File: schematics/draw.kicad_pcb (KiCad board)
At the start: 2 copper layers, 50 x 40 mm, 38 parts, among them P1 I2C, P2 UART, P3 DBG, P4 USB_OTG, P5 Power_IN, P6 Power_OUT, SW1 SW_Push, U1 EFM32HG309, U2 TPD4E002, U3 INA260

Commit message: updated silkscreen bumped version
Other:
- board text added: "In"
- board text added: "Out"
- board text added: "draw v1.1 14/3/2017"
- board text added: "↑"
- board text removed: "draw v1.0 7/2/2017"
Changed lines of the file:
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@@
     (area 50.811981 93.5356 116.824543 136.5614)
     (thickness 1.6)
-    (drawings 22)
+    (drawings 25)
     (tracks 268)
     (zones 0)
@@
   (layers
     (0 F.Cu signal)
-    (31 B.Cu signal hide)
+    (31 B.Cu signal)
     (32 B.Adhes user)
     (33 F.Adhes user)
@@
       (xy 0.376964 2.709982)) (layer B.SilkS) (width 0.01))
   )
-  (gr_text "draw v1.0\n7/2/2017" (at 64.5922 124.4981) (layer B.SilkS)
+  (gr_text Out (at 63.119 105.791) (layer F.SilkS)
+    (effects (font (size 1.2 1.2) (thickness 0.3)))
+  )
+  (gr_text In (at 63.2079 125.5268) (layer F.SilkS)
+    (effects (font (size 1.2 1.2) (thickness 0.3)))
+  )
+  (gr_text ↑ (at 64.262 113.3221) (layer F.SilkS)
+    (effects (font (size 7.2 1.2) (thickness 0.3)))
+  )
+  (gr_text "draw v1.1\n14/3/2017" (at 64.5922 124.4981) (layer B.SilkS)
     (effects (font (size 0.8 0.8) (thickness 0.2)) (justify mirror))
   )

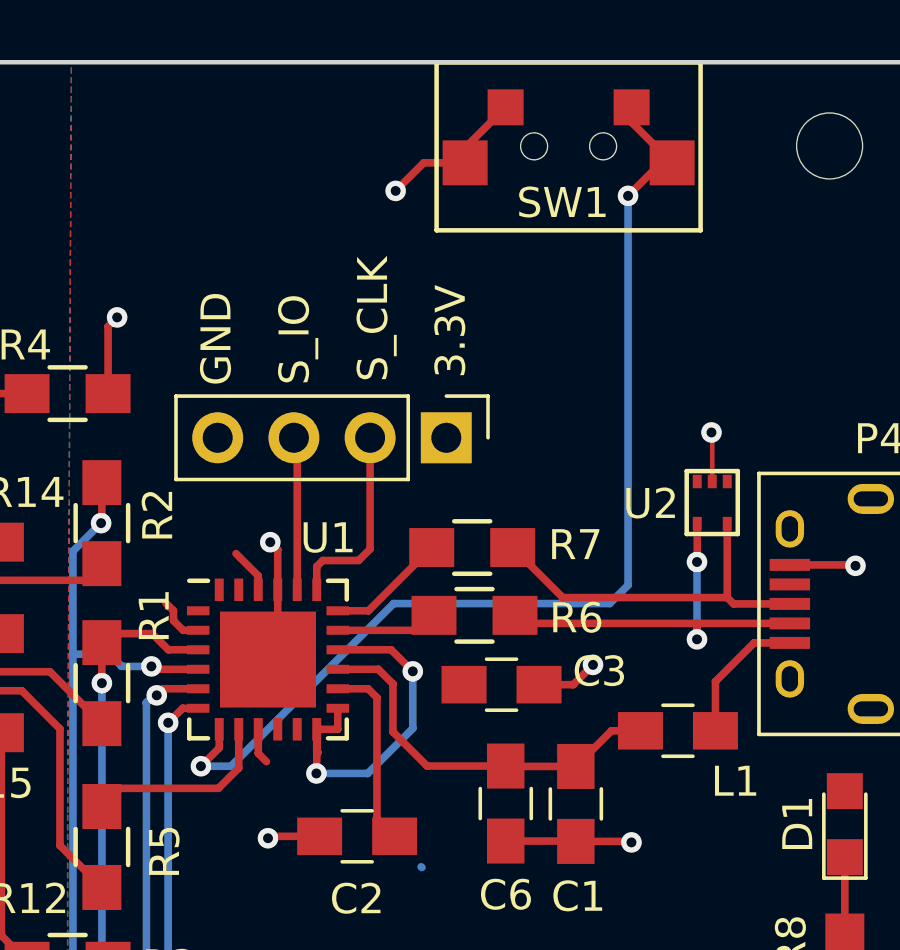
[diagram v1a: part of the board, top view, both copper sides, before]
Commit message: fixed the footprint for button
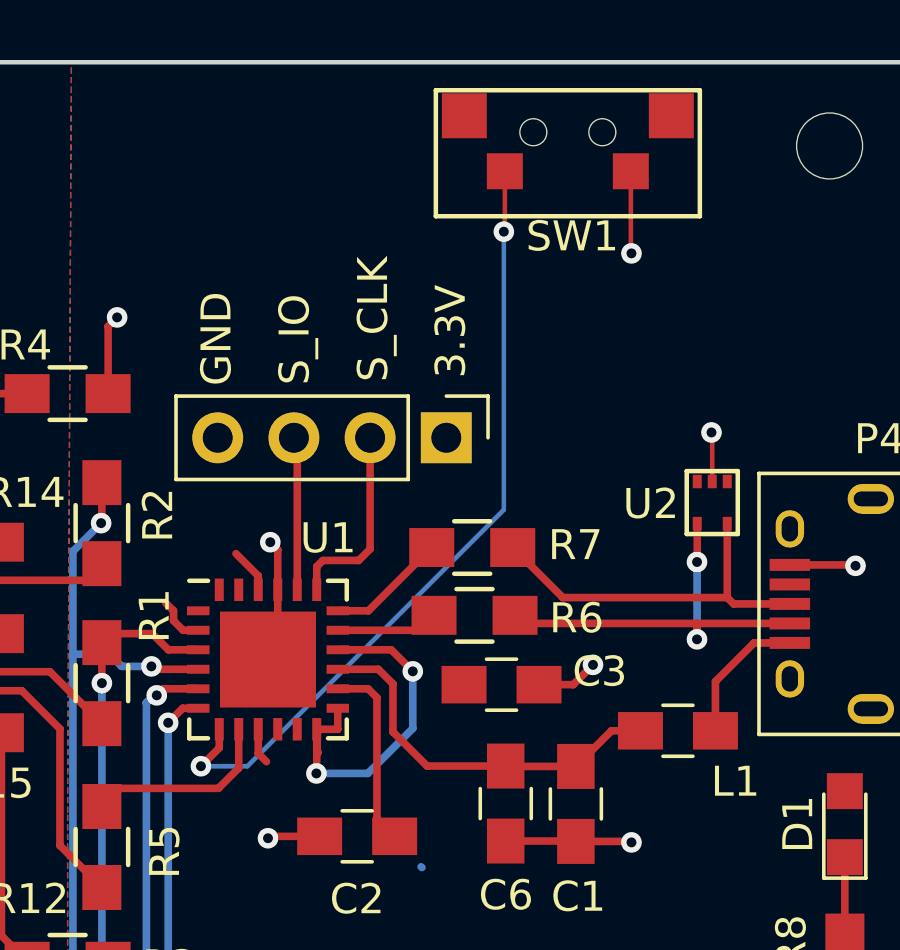
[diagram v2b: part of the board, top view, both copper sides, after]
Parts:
- SW1: footprint draw:HTB1 -> draw:Tact
- moved SW1 0.47 mm to (98.5, 97.3), turned to 0 degrees
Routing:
- net Net-(SW1-Pad1): track 35.6 -> 26.5 mm
- net GND: track 30.5 -> 28.1 mm
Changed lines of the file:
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@@
 (kicad_pcb (version 4) (host pcbnew 4.0.5)
   (general
-    (links 88)
+    (links 86)
     (no_connects 0)
     (area 50.811981 93.5356 116.824543 136.5614)
     (thickness 1.6)
     (drawings 25)
-    (tracks 268)
+    (tracks 261)
     (zones 0)
     (modules 38)
@@
   (page A4)
   (layers
-    (0 F.Cu signal)
+    (0 F.Cu signal hide)
     (31 B.Cu signal)
     (32 B.Adhes user)
@@
   )
   (setup
-    (last_trace_width 0.254)
+    (last_trace_width 0.1524)
     (user_trace_width 0.1524)
     (user_trace_width 1.1)
@@
     (add_net "Net-(U2-Pad3)")
     (add_net "Net-(U3-Pad13)")
-  )
-  (module draw:HTB1 (layer F.Cu)
-    (at 98.4885 97.8027 180)
-    (fp_text reference SW1 (at 0.1905 -1.8923 180) (layer F.SilkS)
-      (effects (font (size 1 1) (thickness 0.15)))
-    )
-    (fp_text value SW_Push (at 0 -1.905 180) (layer F.Fab) hide
-      (effects (font (size 1 1) (thickness 0.15)))
-    )
-    (fp_line (start -4.4 -2.8) (end 4.4 -2.8) (layer F.SilkS) (width 0.15))
-    (fp_line (start 4.4 -2.8) (end 4.4 2.8) (layer F.SilkS) (width 0.15))
-    (fp_line (start 4.4 2.8) (end -4.4 2.8) (layer F.SilkS) (width 0.15))
-    (fp_line (start -4.4 2.8) (end -4.4 -2.8) (layer F.SilkS) (width 0.15))
-    (pad 2 smd rect (at 3.45 -0.55 180) (size 1.5 1.5) (layers F.Cu F.Paste F.Mask)
-      (net 2 GND))
-    (pad "" np_thru_hole circle (at -1.15 0 180) (size 0.9 0.9) (drill 0.9) (layers *.Cu *.Mask))
-    (pad 2 smd rect (at 2.1 1.3 180) (size 1.2 1.2) (layers F.Cu F.Paste F.Mask)
-      (net 2 GND))
-    (pad 1 smd rect (at -2.1 1.3 180) (size 1.2 1.2) (layers F.Cu F.Paste F.Mask)
-      (net 25 "Net-(SW1-Pad1)"))
-    (pad "" np_thru_hole circle (at 1.15 0 180) (size 0.9 0.9) (drill 0.9) (layers *.Cu *.Mask))
-    (pad 1 smd rect (at -3.45 -0.55 180) (size 1.5 1.5) (layers F.Cu F.Paste F.Mask)
-      (net 25 "Net-(SW1-Pad1)"))
   )
   (module Resistors_SMD:R_0805_HandSoldering (layer F.Cu)
@@
       (xy 0.376964 2.709982)) (layer B.SilkS) (width 0.01))
   )
+  (module draw:Tact (layer F.Cu)
+    (at 98.4631 97.3328)
+    (fp_text reference SW1 (at 0.15 3.475) (layer F.SilkS)
+      (effects (font (size 1 1) (thickness 0.15)))
+    )
+    (fp_text value SW_Push (at -0.05 2) (layer F.Fab)
+      (effects (font (size 1 1) (thickness 0.15)))
+    )
+    (fp_line (start -4.4 -1.4) (end 4.4 -1.4) (layer F.SilkS) (width 0.15))
+    (fp_line (start 4.4 -1.4) (end 4.4 2.8) (layer F.SilkS) (width 0.15))
+    (fp_line (start 4.4 2.8) (end -4.4 2.8) (layer F.SilkS) (width 0.15))
+    (fp_line (start -4.4 2.8) (end -4.4 -1.4) (layer F.SilkS) (width 0.15))
+    (pad "" smd rect (at 3.45 -0.55) (size 1.5 1.5) (layers F.Cu F.Paste F.Mask))
+    (pad "" np_thru_hole circle (at -1.15 0) (size 0.9 0.9) (drill 0.9) (layers *.Cu *.Mask))
+    (pad 2 smd rect (at 2.1 1.3) (size 1.2 1.2) (layers F.Cu F.Paste F.Mask)
+      (net 2 GND))
+    (pad 1 smd rect (at -2.1 1.3) (size 1.2 1.2) (layers F.Cu F.Paste F.Mask)
+      (net 25 "Net-(SW1-Pad1)"))
+    (pad "" np_thru_hole circle (at 1.15 0) (size 0.9 0.9) (drill 0.9) (layers *.Cu *.Mask))
+    (pad "" smd rect (at -3.45 -0.55) (size 1.5 1.5) (layers F.Cu F.Paste F.Mask))
+  )
   (gr_text Out (at 63.119 105.791) (layer F.SilkS)
     (effects (font (size 1.2 1.2) (thickness 0.3)))
@@
   (segment (start 100.8834 117.2845) (end 99.9182 117.2845) (width 0.254) (layer F.Cu) (net 1))
   (segment (start 99.9182 117.2845) (end 98.7298 118.4729) (width 0.254) (layer F.Cu) (net 1))
-  (segment (start 95.0385 98.3527) (end 95.0385 97.8527) (width 0.254) (layer F.Cu) (net 2))
-  (segment (start 95.0385 97.8527) (end 96.3885 96.5027) (width 0.254) (layer F.Cu) (net 2))
-  (segment (start 95.0385 98.3527) (end 93.6586 98.3527) (width 0.254) (layer F.Cu) (net 2))
-  (segment (start 92.7227 99.2886) (end 92.7227 99.3394) (width 0.254) (layer B.Cu) (net 2))
-  (via (at 92.7227 99.2886) (size 0.6858) (drill 0.3302) (layers F.Cu B.Cu) (net 2))
-  (segment (start 93.6586 98.3527) (end 92.7227 99.2886) (width 0.254) (layer F.Cu) (net 2))
+  (segment (start 100.5631 98.6328) (end 100.5631 101.3505) (width 0.1524) (layer F.Cu) (net 2) (status 400000))
+  (via (at 100.584 101.3714) (size 0.6858) (drill 0.3302) (layers F.Cu B.Cu) (net 2))
+  (segment (start 100.5631 101.3505) (end 100.584 101.3714) (width 0.1524) (layer F.Cu) (net 2))
   (segment (start 97.5033 115.7478) (end 98.6409 115.7478) (width 0.254) (layer F.Cu) (net 2))
   (via (at 99.3013 115.0874) (size 0.6858) (drill 0.3302) (layers F.Cu B.Cu) (net 2))
@@
   (segment (start 72.4916 119.3038) (end 74.168 119.3038) (width 0.254) (layer F.Cu) (net 24))
   (segment (start 71.445 118.2572) (end 72.4916 119.3038) (width 0.254) (layer F.Cu) (net 24))
-  (segment (start 100.4697 112.4331) (end 100.4697 99.4537) (width 0.254) (layer B.Cu) (net 25))
-  (segment (start 87.2363 118.4656) (end 92.6592 113.0427) (width 0.254) (layer B.Cu) (net 25))
-  (segment (start 92.6592 113.0427) (end 99.8601 113.0427) (width 0.254) (layer B.Cu) (net 25))
-  (segment (start 99.8601 113.0427) (end 100.4697 112.4331) (width 0.254) (layer B.Cu) (net 25))
-  (segment (start 86.233 118.4656) (end 87.2363 118.4656) (width 0.254) (layer B.Cu) (net 25))
-  (segment (start 100.4697 99.4537) (end 101.5707 98.3527) (width 0.254) (layer F.Cu) (net 25))
-  (via (at 100.4697 99.4537) (size 0.6858) (drill 0.3302) (layers F.Cu B.Cu) (net 25))
-  (segment (start 101.5707 98.3527) (end 101.9385 98.3527) (width 0.254) (layer F.Cu) (net 25))
+  (segment (start 86.233 118.4656) (end 87.7824 118.4656) (width 0.1524) (layer B.Cu) (net 25))
+  (segment (start 96.3631 100.6139) (end 96.3631 98.6328) (width 0.1524) (layer F.Cu) (net 25) (status 800000))
+  (segment (start 96.3295 100.6475) (end 96.3631 100.6139) (width 0.1524) (layer F.Cu) (net 25))
+  (via (at 96.3295 100.6475) (size 0.6858) (drill 0.3302) (layers F.Cu B.Cu) (net 25))
+  (segment (start 96.3295 109.9185) (end 96.3295 100.6475) (width 0.1524) (layer B.Cu) (net 25))
+  (segment (start 87.7824 118.4656) (end 96.3295 109.9185) (width 0.1524) (layer B.Cu) (net 25))
   (segment (start 86.8432 117.2346) (end 86.8432 117.8554) (width 0.254) (layer F.Cu) (net 25))
   (segment (start 86.2584 118.4402) (end 86.2711 118.4402) (width 0.254) (layer B.Cu) (net 25))
@@
   (via (at 86.233 118.4656) (size 0.6858) (drill 0.3302) (layers F.Cu B.Cu) (net 25))
   (segment (start 86.8432 117.8554) (end 86.233 118.4656) (width 0.254) (layer F.Cu) (net 25))
-  (segment (start 100.5885 96.5027) (end 100.5885 97.0027) (width 0.254) (layer F.Cu) (net 25))
-  (segment (start 100.5885 97.0027) (end 101.9385 98.3527) (width 0.254) (layer F.Cu) (net 25))
   (segment (start 69.495 110.588) (end 70.145 110.588) (width 0.254) (layer F.Cu) (net 34))
   (segment (start 79.582 117.348) (end 79.582 124.112) (width 0.254) (layer F.Cu) (net 35))

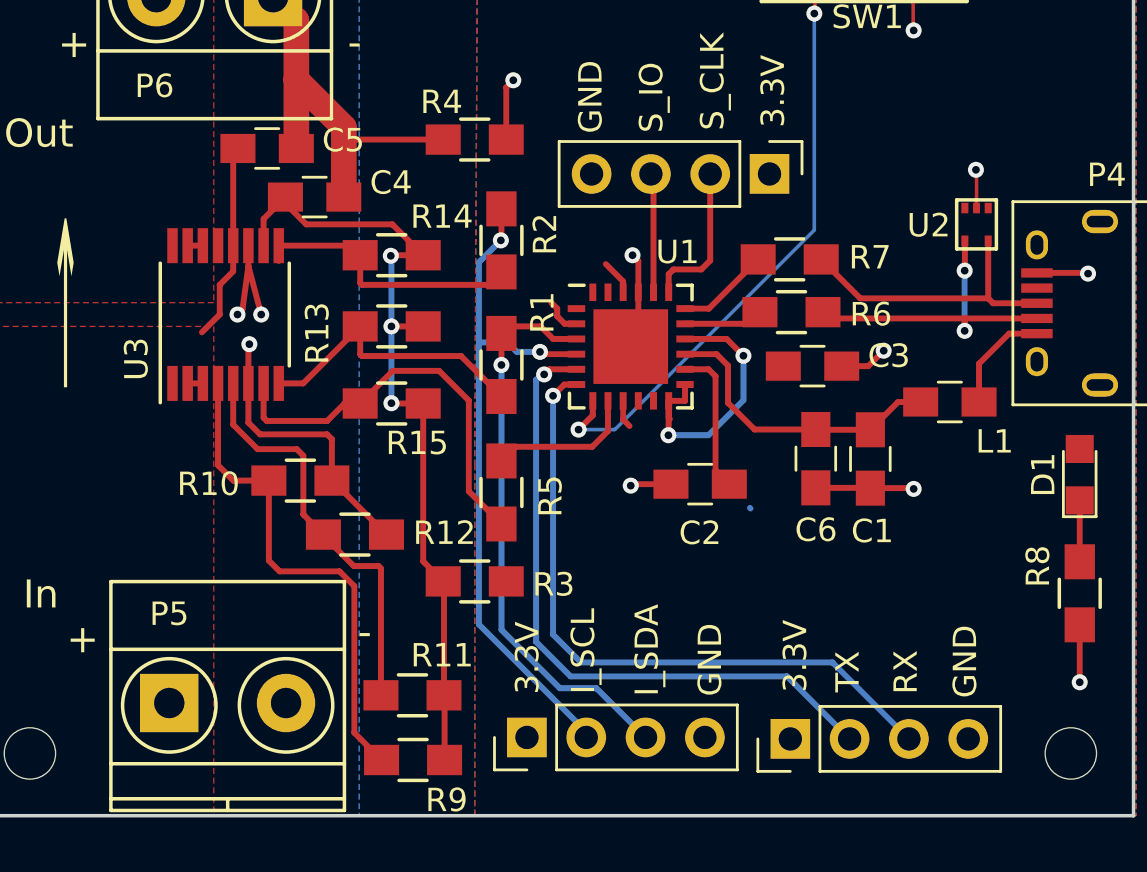
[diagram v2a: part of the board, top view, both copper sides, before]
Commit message: updated to work in kicad 5.1
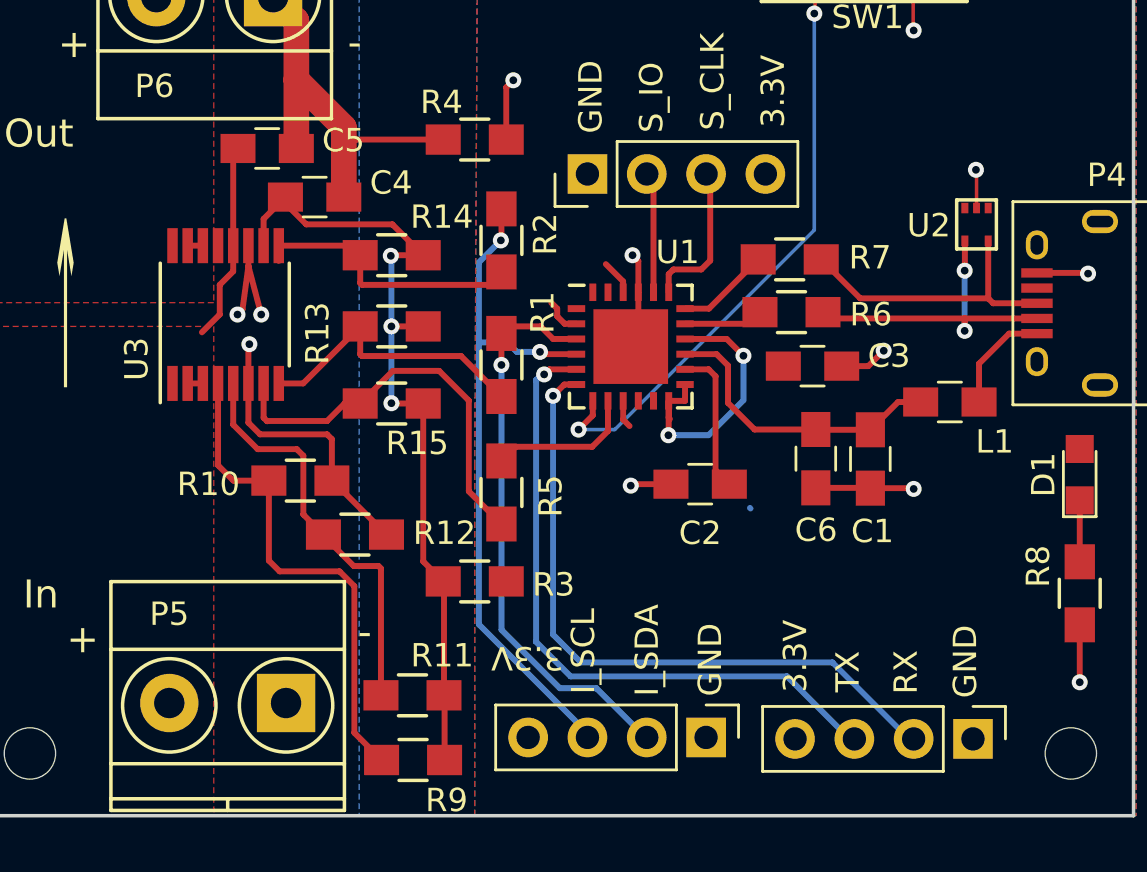
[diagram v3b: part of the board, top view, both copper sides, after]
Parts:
- P1: value I2C -> I2C Conn
- P2: value UART -> UART Conn
- P3: value DBG -> Debug Conn
- R11, R9: value NP -> 0R_NP
- moved P2 7.82 mm to (103.1, 131.7), turned to 270 degrees
- moved P3 7.80 mm to (86.6, 107.5), turned to 90 degrees
- moved P1 7.67 mm to (91.7, 131.6), turned to 270 degrees
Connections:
- P1 pad 1: +3V3 -> GND
- P1 pad 2: /MCU/I2C0_SCL -> /MCU/I2C0-SDA
- P1 pad 3: /MCU/I2C0-SDA -> /MCU/I2C0_SCL
- P1 pad 4: GND -> +3V3
- P2 pad 1: +3V3 -> GND
- P2 pad 2: /MCU/UART_TX -> Net-(P2-Pad2)
- P2 pad 3: Net-(P2-Pad3) -> /MCU/UART_TX
- P2 pad 4: GND -> +3V3
- P3 pad 1: +3V3 -> GND
- P3 pad 2: /MCU/SWD_CLK -> Net-(P3-Pad2)
- P3 pad 3: Net-(P3-Pad3) -> /MCU/SWD_CLK
- P3 pad 4: GND -> +3V3
- U1 pad 20: Net-(P3-Pad3) -> Net-(P3-Pad2)
- U1 pad 6: Net-(P2-Pad3) -> Net-(P2-Pad2)
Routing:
- net Net-(P2-Pad3): track 28.5 -> 0.00 mm, vias 1 -> 0
- net Net-(P2-Pad2): track 0.00 -> 28.5 mm, vias 0 -> 1
- net Net-(P3-Pad3): track 5.11 -> 0.00 mm
- net Net-(P3-Pad2): track 0.00 -> 5.11 mm
